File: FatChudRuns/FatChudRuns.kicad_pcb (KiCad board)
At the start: 4 copper layers, 86.9 x 54.9 mm, 112 parts, among them J1 RJ45_Pulse_JXD6-0001NL, J2 Z-21320110021001, J3 FTSH-107-01-L-DV-K-P, J4 TYPE-C-31-M-12, SW1 TS-1187A-B-A-B, SW5 1825360-3, U1 STM32F107RBT6, U2 DP83848I, U3 USBLC6-2SC6, U4 ST730M33R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

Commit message: routed ETH MDI and magnetics portion with chassis ground. added 0ohm resistors to connect gnd and cgnd
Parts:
- removed the R40 at (150.7, 162.1)
- added C26: 4pF, Capacitor_SMD:C_0603_1608Metric, F.Cu at (102.8, 165.8)
- added C27: 4pF, Capacitor_SMD:C_0603_1608Metric, F.Cu at (102.8, 168.3)
- added R57: 0, Resistor_SMD:R_0603_1608Metric, F.Cu at (102.8, 170.8)
- added R58: 0, Resistor_SMD:R_0603_1608Metric, F.Cu at (248.4, 124.8)
- added R59: 0, Resistor_SMD:R_0603_1608Metric, F.Cu at (248.4, 103.9)
- moved R31 112.9 mm to (215.2, 113.8), turned to 180 degrees
- moved R34 102.4 mm to (215.2, 111.8)
- moved R33 102.1 mm to (215.2, 109.8), turned to 180 degrees
- moved R32 98.1 mm to (215.2, 115.8)
- moved C17 90.9 mm to (222.1, 110.4), turned to 90 degrees
- moved C18 89.7 mm to (222.1, 118.2), turned to -90 degrees
- moved R40 86.0 mm to (220.9, 106.8)
- moved C15 83.5 mm to (215.2, 108.0), turned to 180 degrees
- moved C16 82.1 mm to (215.2, 117.6), turned to 180 degrees
- moved R39 80.2 mm to (222.1, 123.1), turned to 90 degrees
- moved J3 28.6 mm to (195.1, 104.3)
- moved SW5 18.0 mm to (173.6, 140.5)
- moved Y2 15.5 mm to (188.2, 124.4)
- moved U2 7.34 mm to (206.9, 112.5)
- moved U1 4.85 mm to (182.9, 114.0)
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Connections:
- Y2 pad 3: /MCU/OSC_OUT -> Net-(C27-Pad1)
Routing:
- net /ETH_PHY/LED_ACT: track 0.00 -> 31.0 mm, vias 0 -> 2
- net +3.3V: track 0.00 -> 26.7 mm, vias 0 -> 10
- net /ETH_PHY/LED_LINK: track 0.00 -> 21.5 mm
- net GND: track 1.84 -> 12.9 mm, vias 1 -> 9
- net /ETH_PHY/ETH_TD-: track 7.79 -> 18.5 mm
- net /ETH_PHY/ETH_TD+: track 7.79 -> 18.1 mm
- net /ETH_PHY/ETH_RD-: track 7.75 -> 16.2 mm
- net /ETH_PHY/ETH_RD+: track 7.75 -> 16.0 mm
- net Net-(J1-Pad2): track 0.00 -> 5.58 mm
- net Net-(J1-Pad10): track 0.00 -> 4.56 mm
- net CGND: vias 0 -> 23
- added copper zone on In2.Cu, net +3.3V
- added copper zone on B.Cu, net CGND
- added copper zone on F.Cu, net CGND
- added copper zone on In1.Cu, net CGND

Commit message: added one more decoup cap for eth phy (another power pin), routed decoup caps, routed phy filter resistors
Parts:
- removed the C11 at (142.3, 131.1)
- removed the C19 at (142.3, 134.1)
- removed the C9 at (142.3, 128.1)
- C11, C12, C13, C20, C9, R36, R37, R46: moved to B.Cu
- C28: value ~ -> 100nF
- U2: footprint Package_QFP:LQFP-48_7x7mm_P0.5mm -> Package_QFP:LQFP-48-1EP_7x7mm_P0.5mm_EP3.6x3.6mm_ThermalVias
- moved C28 112.7 mm to (199.1, 115.6), turned to 90 degrees
- moved C9 110.5 mm to (210.2, 108.5), turned to 90 degrees
- moved C11 107.3 mm to (206.3, 108.5), turned to 90 degrees
- moved R35 106.9 mm to (214.5, 105.0), turned to 180 degrees
- moved C19 106.9 mm to (203.9, 103.9), turned to 180 degrees
- moved R37 105.8 mm to (214.7, 112.3)
- moved R36 103.5 mm to (214.8, 114.0)
- moved C13 83.9 mm to (212.0, 114.8), turned to -90 degrees
- moved C12 81.1 mm to (208.2, 108.5), turned to 90 degrees
- moved R46 80.0 mm to (214.2, 110.7), turned to 180 degrees
- moved C10 77.0 mm to (203.9, 105.8), turned to 180 degrees
- moved C20 76.3 mm to (211.9, 108.5), turned to 90 degrees
- moved R45 73.9 mm to (205.2, 101.9), turned to 180 degrees
- moved C14 73.9 mm to (199.1, 108.9), turned to 90 degrees
- moved J3 34.8 mm to (197.4, 139.1)
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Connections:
- net Net-(U2-AVDD33) renamed /ETH_PHY/ETH_3.3VA
- C10 pad 1: Net-(C10-Pad1) -> /ETH_PHY/ETH_3.3V
- C19 pad 1: Net-(C10-Pad1) -> /ETH_PHY/ETH_3.3V
- C28 pad 1: GND -> /ETH_PHY/ETH_3.3V
- C28 pad 2: /MCU/OSC_OUT -> GND
- R45 pad 2: Net-(C10-Pad1) -> /ETH_PHY/ETH_3.3V
- U2 pad 32: Net-(C10-Pad1) -> /ETH_PHY/ETH_3.3V
- U2 pad 48: Net-(C10-Pad1) -> /ETH_PHY/ETH_3.3V
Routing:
- net GND: track 12.9 -> 38.9 mm, vias 9 -> 15
- net Net-(U2-PFBIN1): track 0.00 -> 11.6 mm, vias 0 -> 2
- net Net-(R36-Pad1): track 0.00 -> 9.16 mm, vias 0 -> 1
- net /ETH_PHY/ETH_3.3V: track 0.00 -> 8.97 mm, vias 0 -> 4
- net Net-(R37-Pad1): track 0.00 -> 8.30 mm, vias 0 -> 1
- net Net-(U2-RBIAS): track 0.00 -> 6.97 mm
- net /ETH_PHY/LED_ACT: track 31.0 -> 36.3 mm
- net /ETH_PHY/LED_SPEED: track 0.00 -> 4.07 mm, vias 0 -> 1
- net /ETH_PHY/LED_LINK: track 21.5 -> 25.3 mm
- net /ETH_PHY/ETH_TD+: track 18.1 -> 19.9 mm
- net /ETH_PHY/ETH_3.3VA: track 0.00 -> 1.70 mm, vias 0 -> 1
- net /ETH_PHY/ETH_TD-: track 18.5 -> 19.9 mm
- net /ETH_PHY/ETH_RD+: track 16.0 -> 17.3 mm
- net /ETH_PHY/ETH_RD-: track 16.2 -> 17.4 mm
- net +3.3VA: vias 0 -> 2
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- added copper zone on F.Cu, net +3.3V
- added copper zone on B.Cu, net +3.3VA
- added copper zone on B.Cu, net /ETH_PHY/ETH_3.3V
- added copper zone on F.Cu, net /ETH_PHY/ETH_3.3V
- added copper zone on B.Cu, net /ETH_PHY/ETH_3.3VA

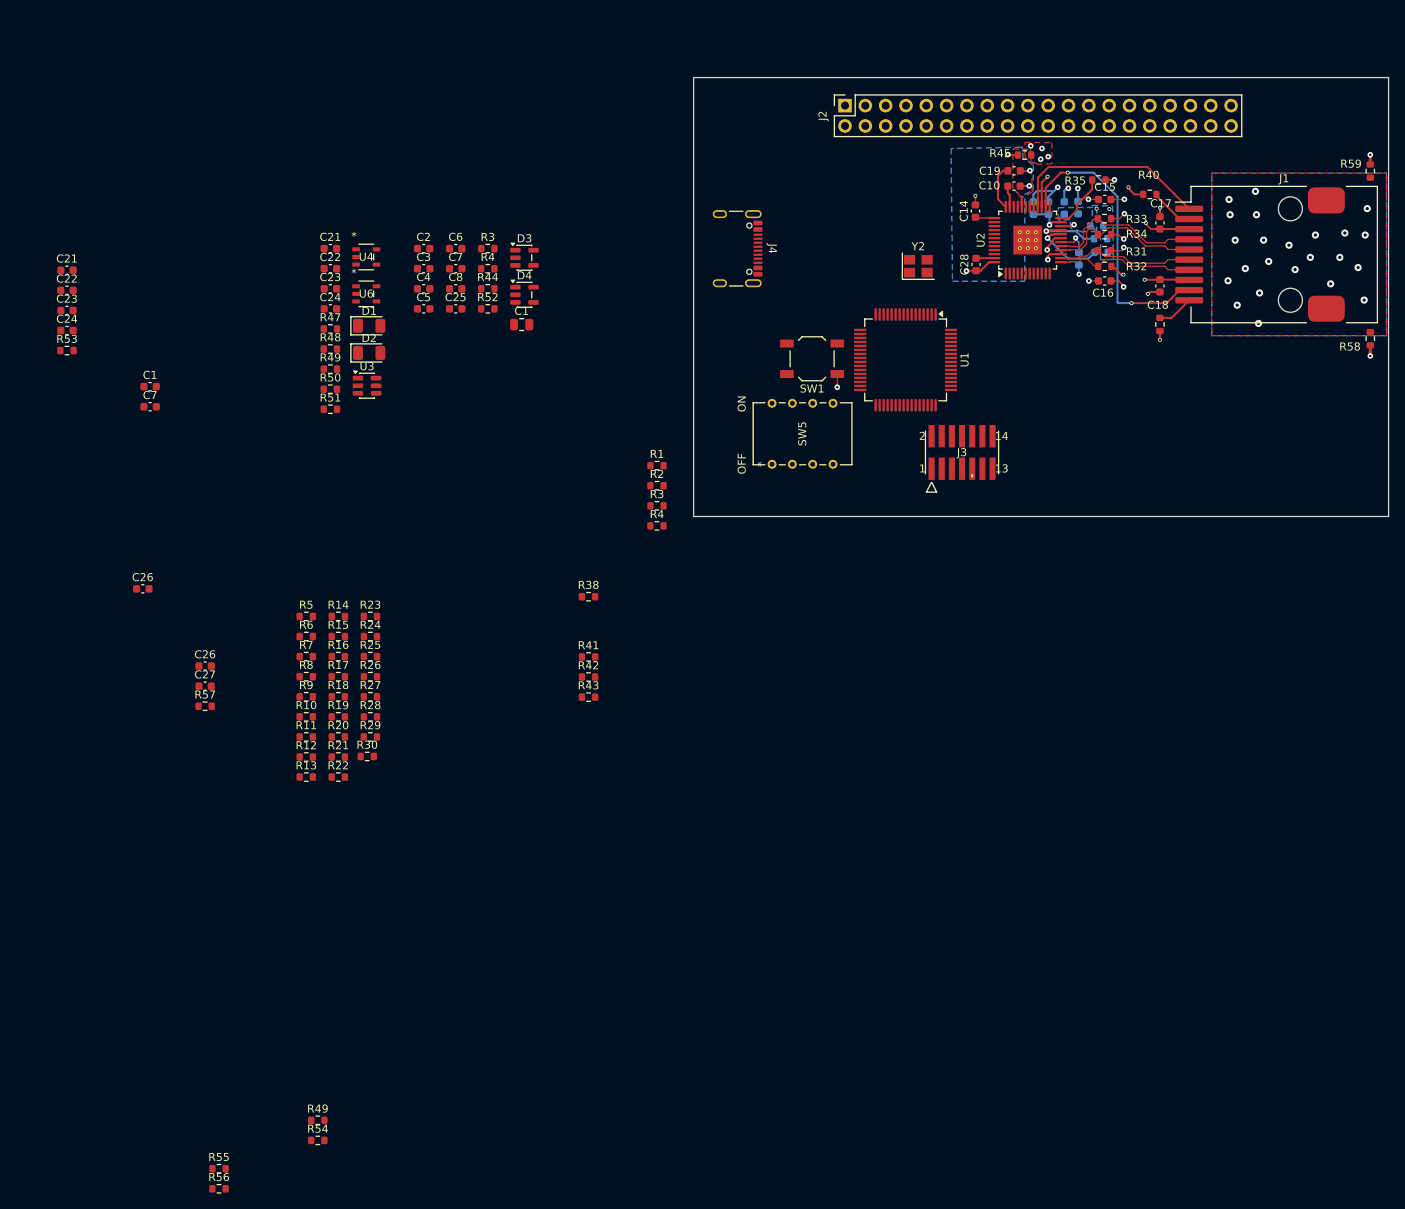
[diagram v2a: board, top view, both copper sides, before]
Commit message: routed phy usb and clock
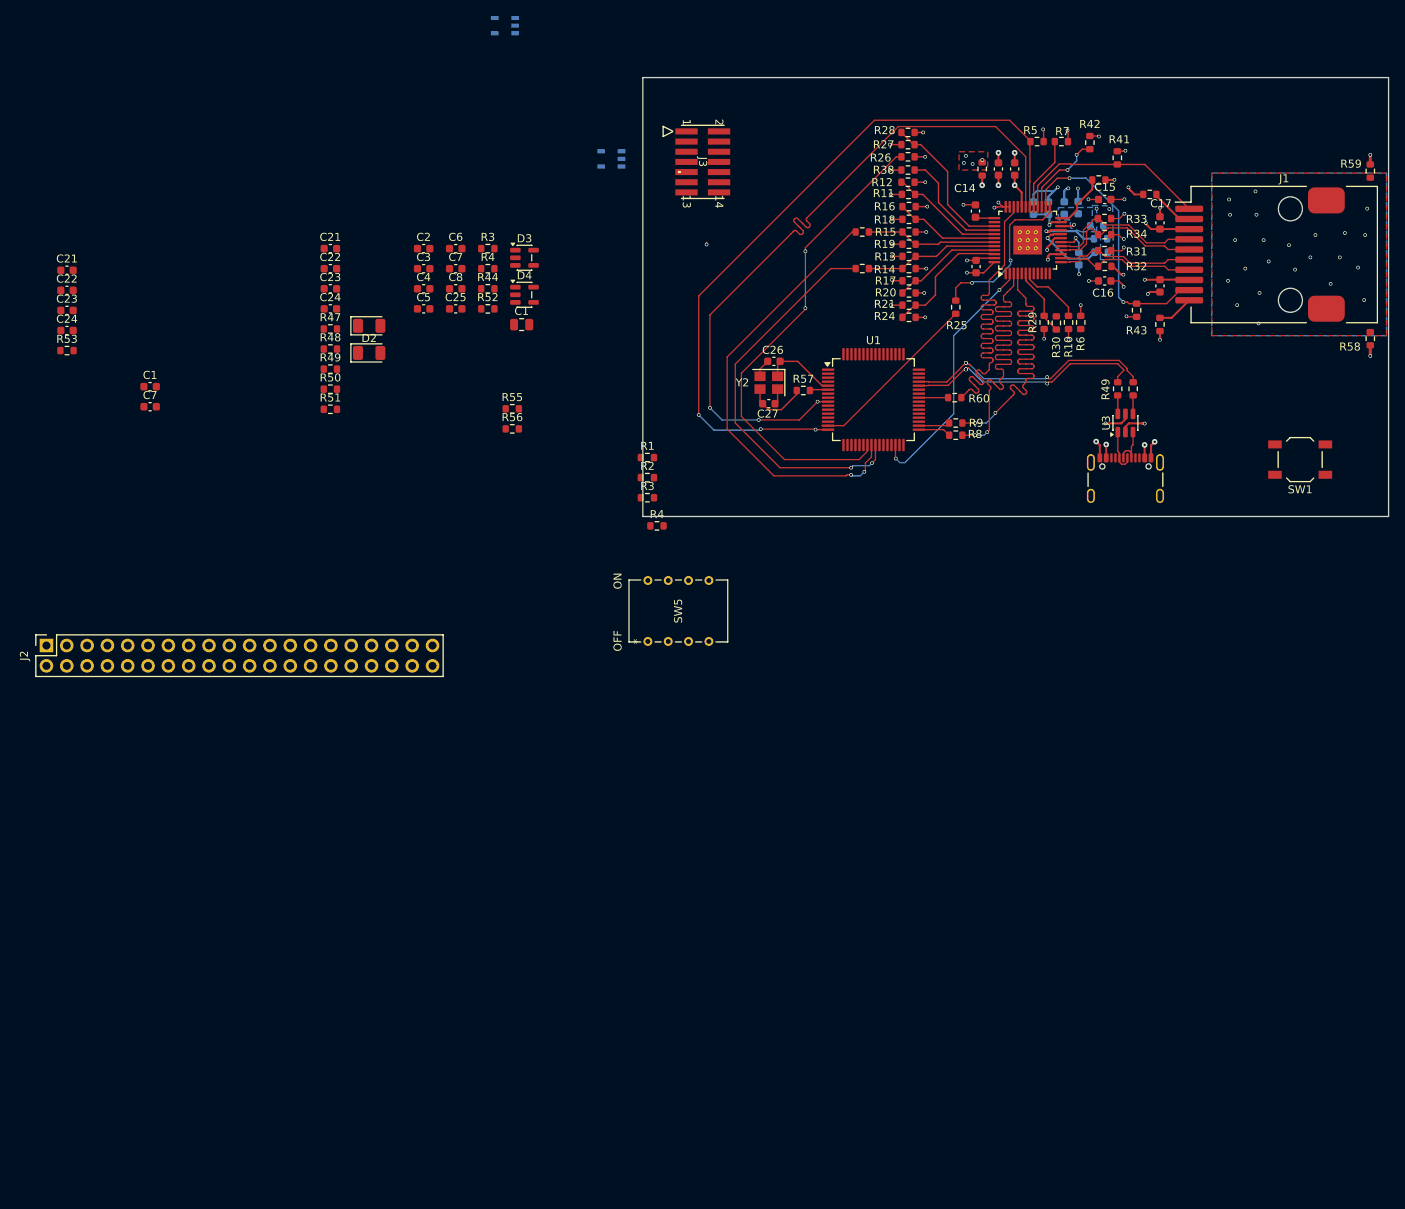
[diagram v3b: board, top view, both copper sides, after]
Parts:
- removed the C26 at (95.0, 156.1)
- added R60: 0, Resistor_SMD:R_0603_1608Metric, F.Cu at (196.5, 132.2)
- U4, U6: moved to B.Cu
- moved R54 138.6 mm to (218.8, 131.1), turned to 90 degrees
- moved R49 135.5 mm to (216.8, 131.1), turned to 90 degrees
- moved J2 120.5 mm to (82.9, 163.2)
- moved R7 114.3 mm to (209.8, 100.2), turned to 180 degrees
- moved R5 108.9 mm to (206.8, 100.2), turned to 180 degrees
- moved R10 107.3 mm to (210.7, 122.8), turned to 90 degrees
- moved R6 104.5 mm to (212.2, 122.8), turned to 90 degrees
- moved R12 104.0 mm to (190.6, 105.3)
- moved R56 101.8 mm to (141.2, 136.1)
- moved R55 101.8 mm to (141.2, 133.6)
- moved R30 101.8 mm to (209.2, 122.9), turned to 90 degrees
- moved R11 101.3 mm to (190.7, 106.8)
- moved R13 99.6 mm to (190.8, 114.6)
- moved R28 99.3 mm to (190.6, 99.1)
- moved R29 98.9 mm to (207.6, 122.8), turned to 90 degrees
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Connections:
- net Net-(U2-25M_OUT) renamed /ETH_PHY/ETH_REF_CLK_1
- net Net-(U2-TXD_0) renamed /ETH_PHY/ETH_TXD0_1
- net Net-(U2-TXD_1) renamed /ETH_PHY/ETH_TXD1_1
- U2 pad 34: RCC_MCO -> /ETH_PHY/ETH_RCC_MCO
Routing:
- net ETH_MDIO: track 0.00 -> 91.9 mm, vias 0 -> 3
- net ETH_MDC: track 0.00 -> 90.1 mm, vias 0 -> 3
- net ETH_CRS_DV: track 0.00 -> 60.3 mm, vias 0 -> 2
- net ETH_RXD0: track 0.00 -> 55.1 mm, vias 0 -> 2
- net /ETH_PHY/ETH_TXD1_1: track 0.00 -> 53.9 mm, vias 0 -> 2
- net /ETH_PHY/ETH_TXD0_1: track 0.00 -> 52.4 mm, vias 0 -> 2
- net /ETH_PHY/ETH_RCC_MCO: track 0.00 -> 50.6 mm
- net ETH_RXD1: track 0.00 -> 49.4 mm, vias 0 -> 2
- net USB_D+: track 0.00 -> 32.2 mm, vias 0 -> 3
- net ETH_TX_EN: track 0.00 -> 32.1 mm, vias 0 -> 2
- net USB_D-: track 0.00 -> 31.0 mm, vias 0 -> 3
- net ETH_REF_CLK: track 0.00 -> 22.7 mm
- net /ETH_PHY/ETH_REF_CLK_1: track 0.00 -> 21.0 mm, vias 0 -> 2
- net +3.3V: track 26.7 -> 46.6 mm, vias 14 -> 29
- net /ETH_PHY/MII_MODE: track 0.00 -> 18.9 mm
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- added copper zone on In2.Cu, net +5V
- added copper zone on In2.Cu, net /ETH_PHY/ETH_3.3V
- removed copper zone on B.Cu, net /ETH_PHY/ETH_3.3V
- removed copper zone on F.Cu, net /ETH_PHY/ETH_3.3V
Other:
- board size 86.9 x 54.9 mm -> 93.2 x 54.9 mm

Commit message: routed jtag, ldo, switch, reset button, and decoupling caps. only need GPIO signals
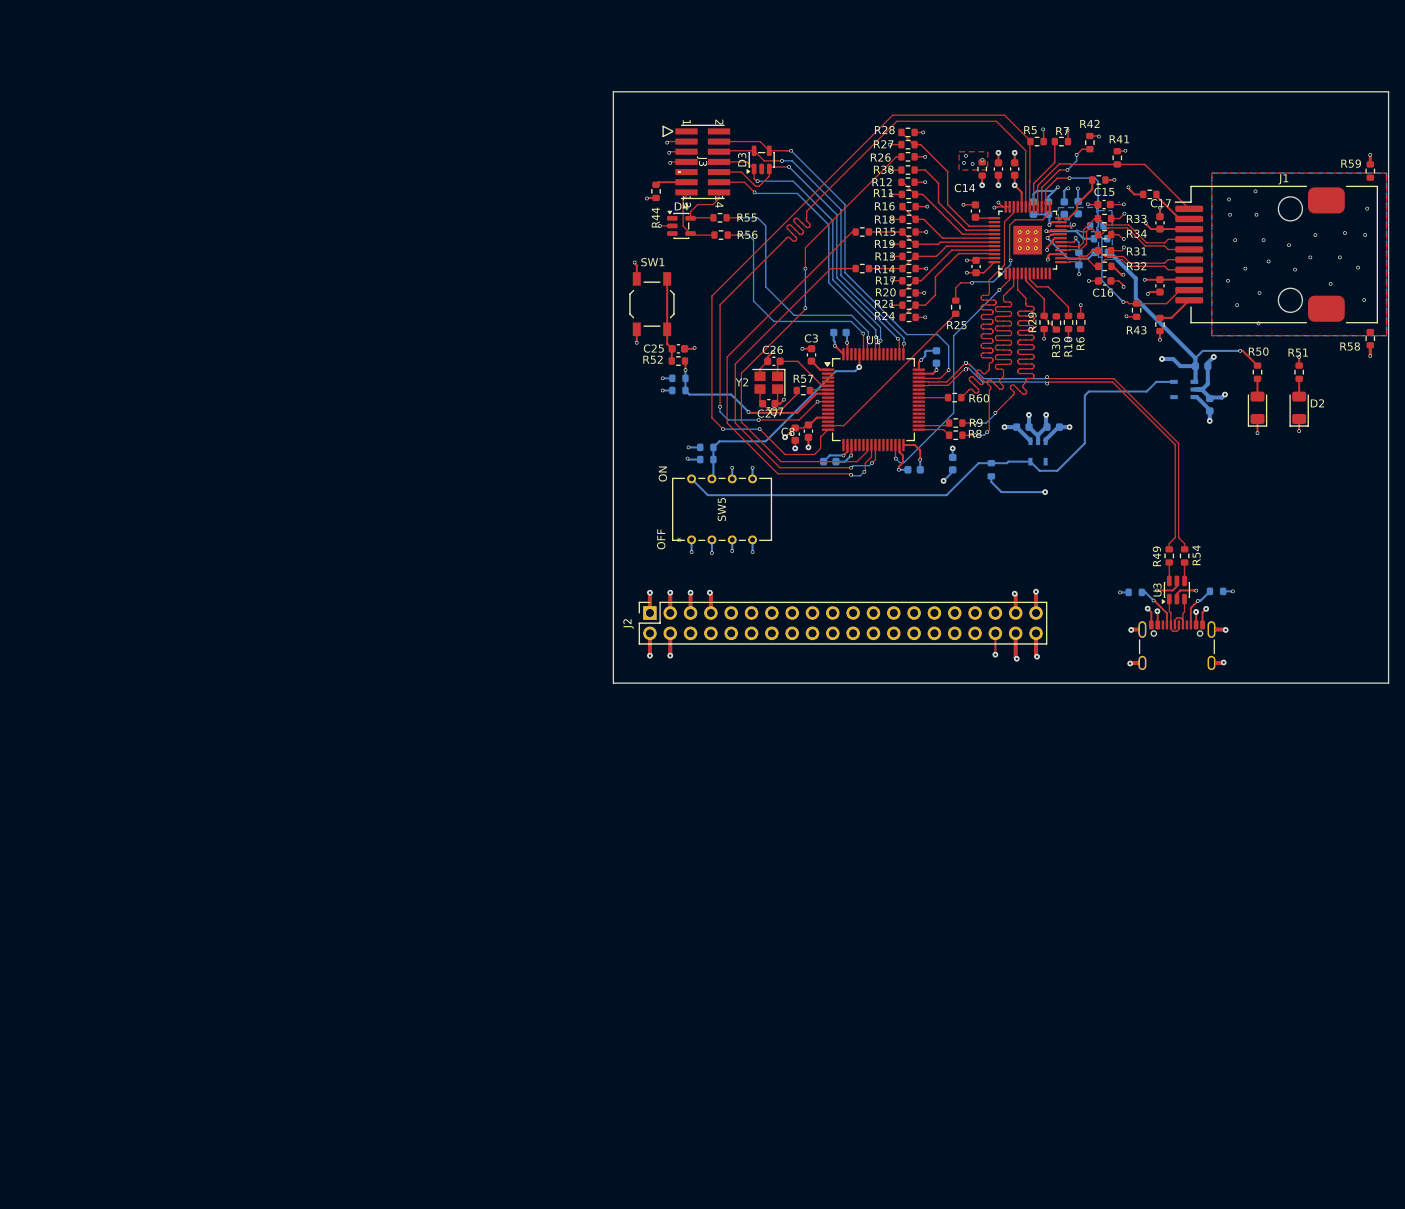
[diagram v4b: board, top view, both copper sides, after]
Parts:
- removed the C1 at (95.9, 130.8)
- removed the C1 at (142.3, 123.1)
- removed the C21 at (118.4, 113.6)
- removed the C21 at (85.5, 116.3)
- removed the C22 at (118.4, 116.1)
- removed the C22 at (85.5, 118.8)
- removed the C23 at (85.5, 121.3)
- removed the C23 at (118.4, 118.6)
- removed the C24 at (85.5, 123.8)
- removed the C24 at (118.4, 121.1)
- removed the C7 at (134.1, 116.1)
- removed the C7 at (95.9, 133.3)
- removed the R3 at (158.1, 144.7)
- removed the R4 at (159.2, 148.2)
- removed the R49 at (118.4, 128.6)
- added C1: 10uF, Capacitor_SMD:C_0603_1608Metric, B.Cu at (196.2, 140.5)
- added C21: 1uF, Capacitor_SMD:C_0603_1608Metric, B.Cu at (208.8, 135.9)
- added C22: 1uF, Capacitor_SMD:C_0603_1608Metric, B.Cu at (205.0, 135.9)
- added C23: 1uF, Capacitor_SMD:C_0603_1608Metric, B.Cu at (228.3, 133.1)
- added C24: 1uF, Capacitor_SMD:C_0603_1608Metric, B.Cu at (227.3, 128.3)
- added C7: 1uF, Capacitor_SMD:C_0603_1608Metric, F.Cu at (176.5, 136.8)
- C2, C4, C5, C6, R1, R2, R3, R4, R47, R48, R53: moved to B.Cu
- moved R51 121.2 mm to (239.5, 129.0), turned to -90 degrees
- moved R53 116.5 mm to (201.0, 141.2), turned to 90 degrees
- moved D2 116.4 mm to (239.5, 133.5), turned to 90 degrees
- moved R50 115.9 mm to (234.3, 129.0), turned to -90 degrees
- moved R47 115.5 mm to (229.2, 156.4)
- moved D1 111.5 mm to (234.3, 133.5), turned to 90 degrees
- moved R48 105.1 mm to (219.0, 156.6), turned to 180 degrees
- moved U6 85.3 mm to (206.9, 138.9), turned to -90 degrees
- moved SW1 83.3 mm to (158.6, 120.5), turned to 90 degrees
- moved U4 77.2 mm to (225.1, 131.2)
- moved J2 75.5 mm to (158.4, 159.1)
- moved C2 67.2 mm to (191.4, 141.2), turned to 180 degrees
- moved C5 64.4 mm to (194.2, 127.1), turned to -90 degrees
- moved C6 53.8 mm to (180.8, 140.2), turned to 180 degrees
- moved C4 52.3 mm to (182.1, 124.1)
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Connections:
- D3 pad 1: /MCU/T_JTDI -> /MCU/T_SWO
- D3 pad 3: /MCU/T_SWO -> /MCU/T_JTDI
- D3 pad 4: /MCU/T_SWCLK -> /MCU/T_SWDIO
- D3 pad 5: /MCU/T_SWDIO -> /MCU/T_SWCLK
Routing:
- net +3.3VA: track 0.00 -> 103.2 mm, vias 2 -> 3
- net GND: track 57.6 -> 144.6 mm, vias 30 -> 71
- net LDO_EN: track 0.00 -> 71.4 mm
- net /MCU/T_SWDIO: track 0.00 -> 51.5 mm, vias 0 -> 2
- net +3.3V: track 46.6 -> 92.0 mm, vias 29 -> 45
- net /MCU/T_JTDI: track 0.00 -> 40.1 mm, vias 0 -> 2
- net /MCU/T_SWCLK: track 0.00 -> 39.7 mm, vias 0 -> 2
- net /MCU/T_SWO: track 0.00 -> 37.2 mm, vias 0 -> 2
- net /MCU/T_NRST: track 0.00 -> 34.6 mm, vias 0 -> 2
- net Net-(U1-PB6): track 0.00 -> 30.9 mm, vias 0 -> 2
- net Net-(U1-PB7): track 0.00 -> 29.1 mm, vias 0 -> 2
- net /MCU/BOOT0: track 0.00 -> 28.0 mm, vias 0 -> 1
- net Net-(U1-NRST): track 0.00 -> 23.7 mm, vias 0 -> 2
- net USB_D-: track 31.0 -> 51.0 mm
- net USB_D+: track 32.2 -> 52.2 mm
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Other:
- board size 93.2 x 54.9 mm -> 96.9 x 73.9 mm
